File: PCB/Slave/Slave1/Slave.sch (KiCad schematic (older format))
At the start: 42 parts, among them J1 Jack-DC, J10 MH, J11 MH, J12 LED1, J13 LED3, J14 LED5, J15 LED2, J16 LED4, J2 GP_IO, J3 PGM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

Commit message: working on the pcb
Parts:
- removed C10, C2: 1µ, Capacitors_SMD:C_0603_HandSoldering, symbol C
- removed J2: GP_IO, Pin_Headers:Pin_Header_Straight_1x04_Pitch2.54mm, symbol Conn_01x04
- removed J7: PIC_IO, Pin_Headers:Pin_Header_Straight_1x05_Pitch2.54mm, symbol Conn_01x05
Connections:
- net B1: now also U4.6 (LED0); no longer U4.8 (LED2)
- net B2: now also U4.9 (LED3); no longer U4.12 (LED5)
- net B3: now also U4.13 (LED6); no longer U4.15 (LED8)
- net B4: now also U4.16 (LED9); no longer U4.18 (LED11)
- net B5: now also U4.20 (LED12); no longer U4.22 (LED14)
- net GND: now also D2.1 (K)
- net MCP_CS: now also U1.11 (~CS)
- net NRF_MISO: no longer U1.14 (SO)
- net NRF_MOSI: no longer U1.13 (SI)
- net R1: now also U4.8 (LED2); no longer U4.6 (LED0)
- net R2: now also U4.12 (LED5); no longer U4.9 (LED3)
- net R3: now also U4.15 (LED8); no longer U4.13 (LED6)
- net R4: now also U4.18 (LED11); no longer U4.16 (LED9)
- net R5: now also U4.22 (LED14); no longer U4.20 (LED12)
- net SEL_MISO: now also U1.14 (SO)
- net SEL_MOSI: now also U1.13 (SI)
- net at R3.2: now also D2.2 (A)
- net IO1: no longer names the net of U3.2 (AN0/OA2OUT/RA0)
- net IO2: no longer names the net of U3.3 (AN1/C2IN1+/RA1)
- net IO3: no longer names the net of U3.9 (OSC1/CLKI/RA2)
- net IO4: no longer names the net of U3.10 (OSC2/CLKO/RA3)
- net IO5: no longer names the net of U3.12 (CV_REF2O_/RP20/T1CK/RA4)
- net SEL1 renamed Select array/SEL1
- net SEL10 renamed Select array/SEL10
- net SEL11 renamed Select array/SEL11
- net SEL12 renamed Select array/SEL12
- net SEL2 renamed Select array/SEL2
- net SEL3 renamed Select array/SEL3
- net SEL4 renamed Select array/SEL4
- net SEL5 renamed Select array/SEL8
- net SEL6 renamed Select array/SEL7
- net SEL7 renamed Select array/SEL6
- net SEL8 renamed Select array/SEL5
- net SEL9 renamed Select array/SEL9
- no-connect marks 6 -> 15
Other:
- moved on the sheet: J12, J13, J14, J15, J16

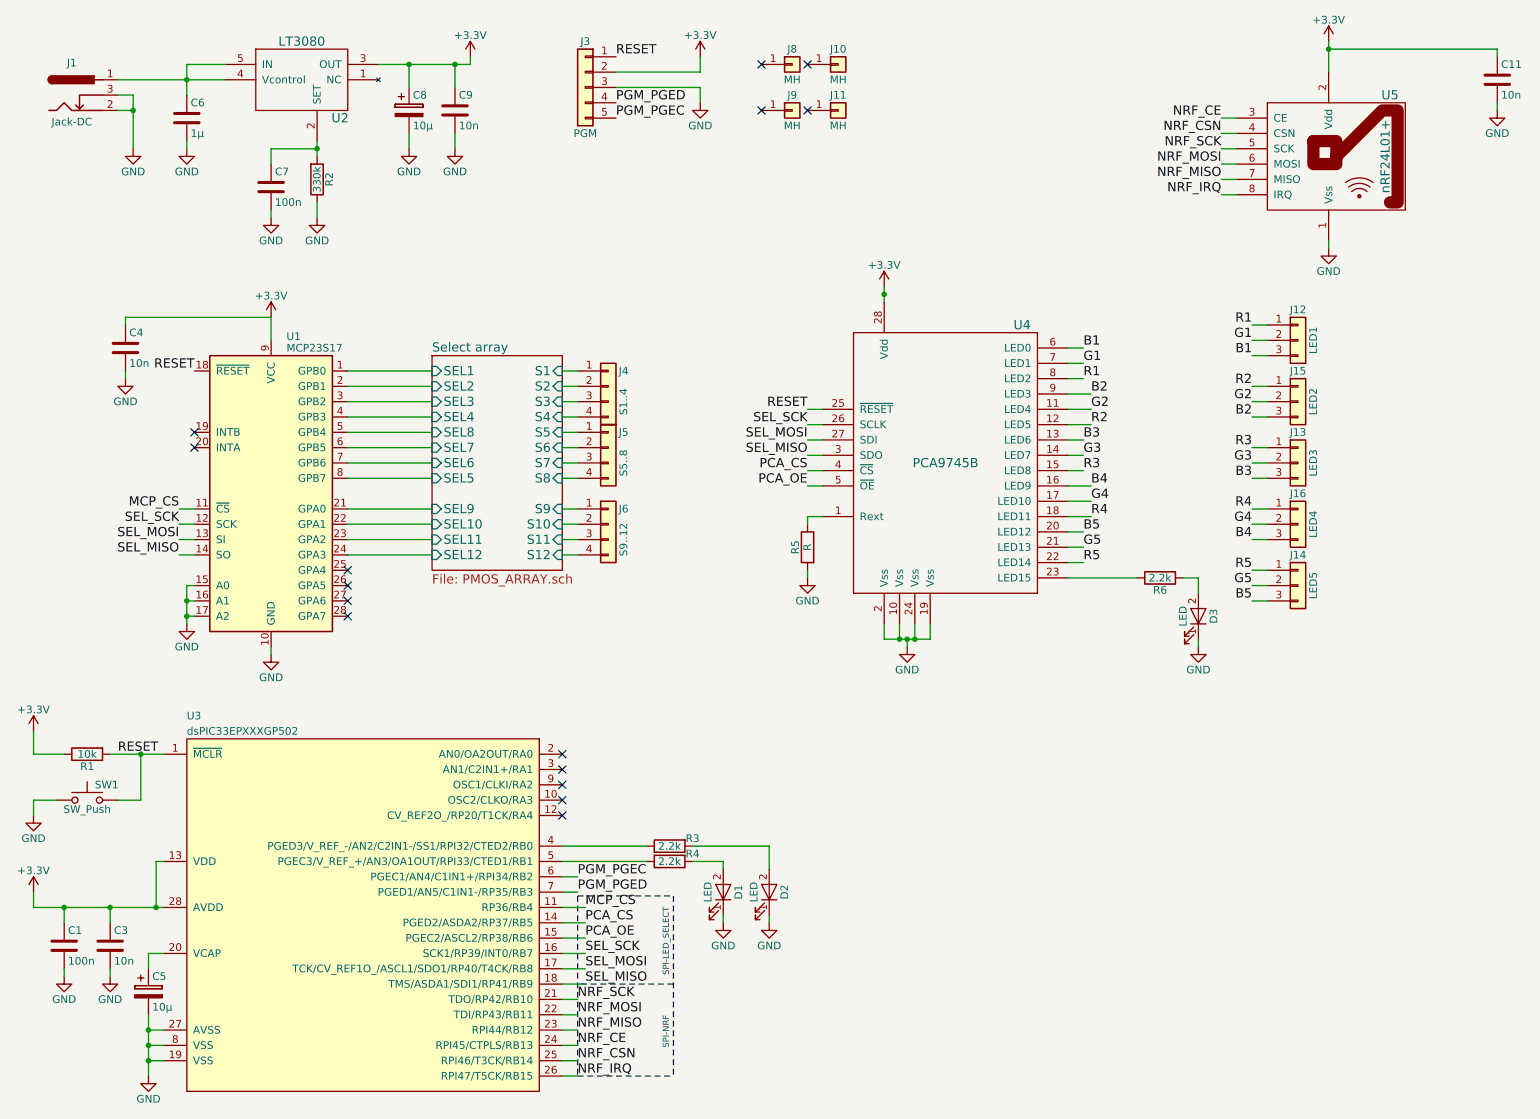
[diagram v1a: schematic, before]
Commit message: created C PIC project for slave
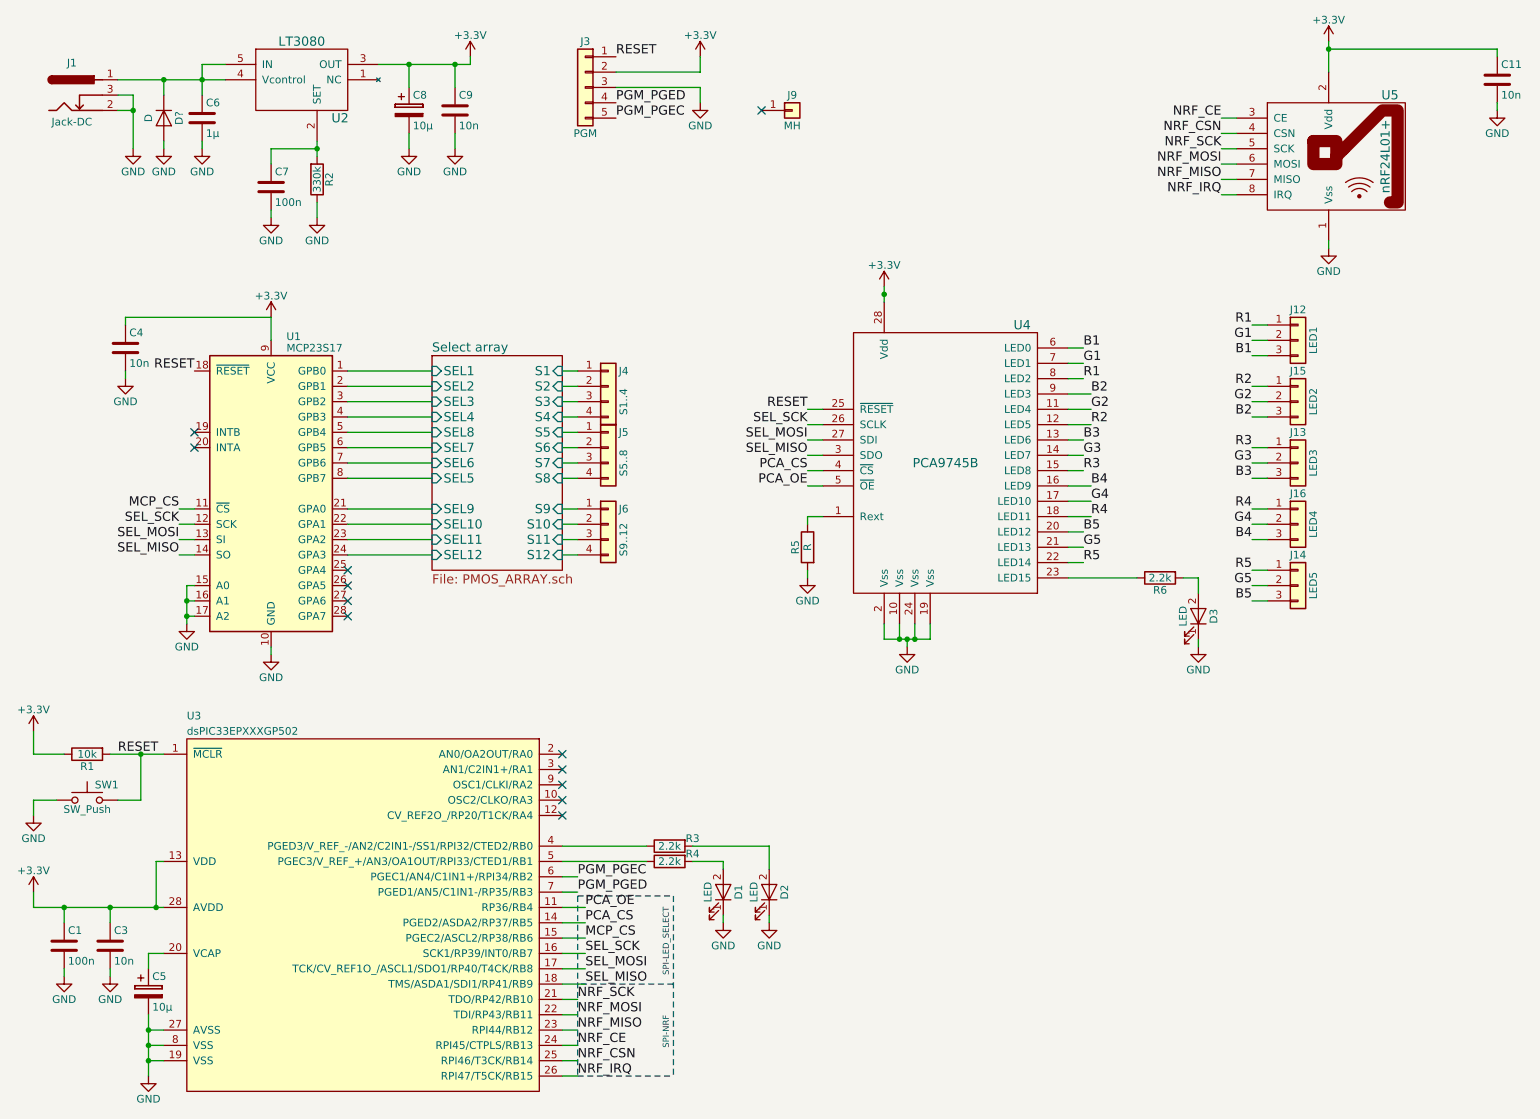
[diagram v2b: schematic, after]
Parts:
- removed J10, J11, J8: MH, Mounting_Holes:MountingHole_2.7mm_M2.5_ISO14580_Pad, symbol Conn_01x01
- added D?: D, Diodes_SMD:D_MicroMELF_Hadsoldering, symbol D
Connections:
- net GND: now also D?.2 (A)
- net MCP_CS: now also U3.15 (PGEC2/ASCL2/RP38/RB6); no longer U3.11 (RP36/RB4)
- net PCA_OE: now also U3.11 (RP36/RB4); no longer U3.15 (PGEC2/ASCL2/RP38/RB6)
- net at C6.1, J1.1, U2.4 (Vcontrol)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: now also D?.1 (K)
- no-connect marks 15 -> 12
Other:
- moved on the sheet: C6
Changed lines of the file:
@@
 Text Label 4500 6550 0    60   ~ 0
 PCA_CS
-Text Label 4500 6650 0    60   ~ 0
+Text Label 4500 6450 0    60   ~ 0
 PCA_OE
 Text Label 5950 3200 2    60   ~ 0
@@
 $EndComp
 $Comp
-L Conn_01x01 J8
-U 1 1 5B16DAF4
-P 5850 950
-F 0 "J8" H 5850 1050 50  0000 C CNN
-F 1 "MH" H 5850 850 50  0000 C CNN
-F 2 "Mounting_Holes:MountingHole_2.7mm_M2.5_ISO14580_Pad" H 5850 950 50  0001 C CNN
-F 3 "" H 5850 950 50  0001 C CNN
-	1    5850 950
-	1    0    0    -1
-$EndComp
-$Comp
-L Conn_01x01 J10
-U 1 1 5B16E03C
-P 6150 950
-F 0 "J10" H 6150 1050 50  0000 C CNN
-F 1 "MH" H 6150 850 50  0000 C CNN
-F 2 "Mounting_Holes:MountingHole_2.7mm_M2.5_ISO14580_Pad" H 6150 950 50  0001 C CNN
-F 3 "" H 6150 950 50  0001 C CNN
-	1    6150 950
-	1    0    0    -1
-$EndComp
-$Comp
 L Conn_01x01 J9
 U 1 1 5B16E0EF
@@
 $EndComp
 $Comp
-L Conn_01x01 J11
-U 1 1 5B16E1A9
-P 6150 1250
-F 0 "J11" H 6150 1350 50  0000 C CNN
-F 1 "MH" H 6150 1150 50  0000 C CNN
-F 2 "Mounting_Holes:MountingHole_2.7mm_M2.5_ISO14580_Pad" H 6150 1250 50  0001 C CNN
-F 3 "" H 6150 1250 50  0001 C CNN
-	1    6150 1250
-	1    0    0    -1
-$EndComp
-$Comp
 L Jack-DC J1
 U 1 1 5B16FEF2
@@
 L C C6
 U 1 1 5B170EA3
-P 1900 1300
-F 0 "C6" H 1925 1400 50  0000 L CNN
-F 1 "1µ" H 1925 1200 50  0000 L CNN
-F 2 "Capacitors_SMD:C_0603_HandSoldering" H 1938 1150 50  0001 C CNN
-F 3 "" H 1900 1300 50  0001 C CNN
-	1    1900 1300
+P 2000 1300
+F 0 "C6" H 2025 1400 50  0000 L CNN
+F 1 "1µ" H 2025 1200 50  0000 L CNN
+F 2 "Capacitors_SMD:C_0603_HandSoldering" H 2038 1150 50  0001 C CNN
+F 3 "" H 2000 1300 50  0001 C CNN
+	1    2000 1300
 	1    0    0    -1
 $EndComp
@@
 L GND #PWR012
 U 1 1 5B171A77
-P 1900 1500
-F 0 "#PWR012" H 1900 1250 50  0001 C CNN
-F 1 "GND" H 1900 1350 50  0000 C CNN
-F 2 "" H 1900 1500 50  0001 C CNN
-F 3 "" H 1900 1500 50  0001 C CNN
-	1    1900 1500
+P 2000 1500
+F 0 "#PWR012" H 2000 1250 50  0001 C CNN
+F 1 "GND" H 2000 1350 50  0000 C CNN
+F 2 "" H 2000 1500 50  0001 C CNN
+F 3 "" H 2000 1500 50  0001 C CNN
+	1    2000 1500
 	1    0    0    -1
 $EndComp
@@
 Text Label 1850 3950 2    60   ~ 0
 SEL_SCK
-Text Label 4500 6450 0    60   ~ 0
+Text Label 4500 6650 0    60   ~ 0
 MCP_CS
 Wire Wire Line
@@
 	1450 1050 2150 1050
 Wire Wire Line
-	2150 950  1900 950
-Wire Wire Line
-	1900 950  1900 1150
-Connection ~ 1900 1050
+	2150 950  2000 950
+Wire Wire Line
+	2000 950  2000 1150
+Connection ~ 2000 1050
 Wire Wire Line
 	3150 950  3750 950
@@
 	3350 1500 3350 1400
 Wire Wire Line
-	1900 1500 1900 1450
+	2000 1500 2000 1450
 Wire Wire Line
 	3750 950  3750 900
@@
 Wire Wire Line
 	4450 4150 4350 4150
-NoConn ~ 5650 950
 NoConn ~ 5650 1250
-NoConn ~ 5950 950
-NoConn ~ 5950 1250
 Wire Wire Line
 	2950 3250 3500 3250
@@
 NoConn ~ 4350 5550
 NoConn ~ 4350 5450
+$Comp
+L D D?
+U 1 1 5B1811C6
+P 1750 1300
+F 0 "D?" H 1750 1400 50  0000 C CNN
+F 1 "D" H 1750 1200 50  0000 C CNN
+F 2 "Diodes_SMD:D_MicroMELF_Hadsoldering" H 1750 1300 50  0001 C CNN
+F 3 "" H 1750 1300 50  0001 C CNN
+	1    1750 1300
+	0    1    1    0
+$EndComp
+$Comp
+L GND #PWR?
+U 1 1 5B1815B1
+P 1750 1500
+F 0 "#PWR?" H 1750 1250 50  0001 C CNN
+F 1 "GND" H 1750 1350 50  0000 C CNN
+F 2 "" H 1750 1500 50  0001 C CNN
+F 3 "" H 1750 1500 50  0001 C CNN
+	1    1750 1500
+	1    0    0    -1
+$EndComp
+Wire Wire Line
+	1750 1500 1750 1450
+Wire Wire Line
+	1750 1150 1750 1050
+Connection ~ 1750 1050
 $EndSCHEMATC

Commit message: better slave pcb
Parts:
- added D17: LED, LEDs:LED_0603_HandSoldering, symbol LED
- added J2: PPIO, Pin_Headers:Pin_Header_Straight_1x04_Pitch2.54mm, symbol Conn_01x04
- added J7: MH, Mounting_Holes:MountingHole_2.7mm_M2.5_ISO14580_Pad, symbol Conn_01x01
- added R43: 2.2k, Resistors_SMD:R_0603_HandSoldering, symbol R
- gave numbers to parts that had none: 1
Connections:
- net GND: now also D17.1 (K)
- net at U3.9 (OSC1/CLKI/RA2): now also R43.1
- net at U1.25 (GPA4): now also J2.1 (Pin_1)
- net at U1.26 (GPA5): now also J2.2 (Pin_2)
- net at U1.27 (GPA6): now also J2.3 (Pin_3)
- net at U1.28 (GPA7): now also J2.4 (Pin_4)
- new net: D17.2 (A), R43.2
- no-connect marks 12 -> 8
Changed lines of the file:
@@
 Wire Wire Line
 	1500 2600 2450 2600
-NoConn ~ 2950 4250
-NoConn ~ 2950 4350
-NoConn ~ 2950 4450
-NoConn ~ 2950 4550
 NoConn ~ 4350 5850
 NoConn ~ 4350 5750
-NoConn ~ 4350 5650
 NoConn ~ 4350 5550
 NoConn ~ 4350 5450
 $Comp
-L D D?
+L D D16
 U 1 1 5B1811C6
 P 1750 1300
-F 0 "D?" H 1750 1400 50  0000 C CNN
+F 0 "D16" H 1750 1400 50  0000 C CNN
 F 1 "D" H 1750 1200 50  0000 C CNN
 F 2 "Diodes_SMD:D_MicroMELF_Hadsoldering" H 1750 1300 50  0001 C CNN
@@
 $EndComp
 $Comp
-L GND #PWR?
+L GND #PWR029
 U 1 1 5B1815B1
 P 1750 1500
-F 0 "#PWR?" H 1750 1250 50  0001 C CNN
+F 0 "#PWR029" H 1750 1250 50  0001 C CNN
 F 1 "GND" H 1750 1350 50  0000 C CNN
 F 2 "" H 1750 1500 50  0001 C CNN
@@
 	1750 1150 1750 1050
 Connection ~ 1750 1050
+$Comp
+L R R43
+U 1 1 5B1E3DB6
+P 5050 5650
+F 0 "R43" V 5000 5500 50  0000 C CNN
+F 1 "2.2k" V 5050 5650 50  0000 C CNN
+F 2 "Resistors_SMD:R_0603_HandSoldering" V 4980 5650 50  0001 C CNN
+F 3 "" H 5050 5650 50  0001 C CNN
+	1    5050 5650
+	0    -1   1    0
+$EndComp
+$Comp
+L LED D17
+U 1 1 5B1E409C
+P 6000 6350
+F 0 "D17" H 6000 6450 50  0000 C CNN
+F 1 "LED" H 6000 6250 50  0000 C CNN
+F 2 "LEDs:LED_0603_HandSoldering" H 6000 6350 50  0001 C CNN
+F 3 "" H 6000 6350 50  0001 C CNN
+	1    6000 6350
+	0    1    -1   0
+$EndComp
+$Comp
+L GND #PWR030
+U 1 1 5B1E41BE
+P 6000 6550
+F 0 "#PWR030" H 6000 6300 50  0001 C CNN
+F 1 "GND" H 6000 6400 50  0000 C CNN
+F 2 "" H 6000 6550 50  0001 C CNN
+F 3 "" H 6000 6550 50  0001 C CNN
+	1    6000 6550
+	1    0    0    -1
+$EndComp
+Wire Wire Line
+	6000 6550 6000 6500
+Wire Wire Line
+	6000 6200 6000 5650
+Wire Wire Line
+	6000 5650 5200 5650
+Wire Wire Line
+	4350 5650 4900 5650
+$Comp
+L Conn_01x04 J2
+U 1 1 5B1E64E5
+P 3250 4350
+F 0 "J2" H 3350 4450 50  0000 C CNN
+F 1 "PPIO" V 3350 4250 50  0000 C CNN
+F 2 "Pin_Headers:Pin_Header_Straight_1x04_Pitch2.54mm" H 3250 4350 50  0001 C CNN
+F 3 "" H 3250 4350 50  0001 C CNN
+	1    3250 4350
+	1    0    0    -1
+$EndComp
+Wire Wire Line
+	3050 4250 2950 4250
+Wire Wire Line
+	2950 4350 3050 4350
+Wire Wire Line
+	2950 4450 3050 4450
+Wire Wire Line
+	2950 4550 3050 4550
+$Comp
+L Conn_01x01 J7
+U 1 1 5B1E7ED5
+P 6250 1250
+F 0 "J7" H 6250 1350 50  0000 C CNN
+F 1 "MH" H 6250 1150 50  0000 C CNN
+F 2 "Mounting_Holes:MountingHole_2.7mm_M2.5_ISO14580_Pad" H 6250 1250 50  0001 C CNN
+F 3 "" H 6250 1250 50  0001 C CNN
+	1    6250 1250
+	1    0    0    -1
+$EndComp
+NoConn ~ 6050 1250
 $EndSCHEMATC

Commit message: updated pcb for prototype
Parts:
- removed J1: Jack-DC, Connect:BARREL_JACK, symbol Jack-DC
- added J1: 5V, Pin_Headers:Pin_Header_Straight_1x02_Pitch2.54mm, symbol Conn_01x02
- added SW2: SW_Push_SPDT, Pin_Headers:Pin_Header_Straight_1x03_Pitch2.54mm, symbol SW_Push_SPDT
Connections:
- net +3V3: now also SW2.1 (A)
- net GND: now also J1.2 (Pin_2)
- net +5V: now reaches C6.1, D16.1 (K), U2.4 (Vcontrol), U2.5 (IN)
- net +5V: now also J1.1 (Pin_1), SW2.3 (C)
- new net Select array/Vdd: SW2.2 (B)
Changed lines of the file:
@@
-$EndComp
-$Comp
-L Jack-DC J1
-U 1 1 5B16FEF2
-P 1150 1150
-F 0 "J1" H 1150 1360 50  0000 C CNN
-F 1 "Jack-DC" H 1150 975 50  0000 C CNN
-F 2 "Connect:BARREL_JACK" H 1200 1110 50  0001 C CNN
-F 3 "" H 1200 1110 50  0001 C CNN
-	1    1150 1150
-	1    0    0    -1
 $EndComp
 $Comp
@@
 	1550 1150 1450 1150
 Wire Wire Line
-	1450 1250 1550 1250
-Connection ~ 1550 1250
-Wire Wire Line
 	1450 1050 2150 1050
 Wire Wire Line
 	2150 950  2000 950
 Wire Wire Line
-	2000 950  2000 1150
+	2000 900  2000 1150
 Connection ~ 2000 1050
 Wire Wire Line
@@
 	5400 6150 5400 6200
 $Sheet
-S 3500 2850 850  1400
+S 3500 2850 850  1500
 U 5B180A3C
 F0 "Select array" 60
@@
 F24 "SEL12" I L 3500 4150 60
 F25 "S12" I R 4350 4150 60
+F26 "Vdd" I R 4350 4300 60
 $EndSheet
 $Comp
@@
 $EndComp
 NoConn ~ 6050 1250
+$Comp
+L +5V #PWR031
+U 1 1 5B45643A
+P 2000 900
+F 0 "#PWR031" H 2000 750 50  0001 C CNN
+F 1 "+5V" H 2000 1040 50  0000 C CNN
+F 2 "" H 2000 900 50  0001 C CNN
+F 3 "" H 2000 900 50  0001 C CNN
+	1    2000 900
+	1    0    0    -1
+$EndComp
+Connection ~ 2000 950
+$Comp
+L SW_Push_SPDT SW2
+U 1 1 5B456FB5
+P 4950 4300
+F 0 "SW2" H 4950 4470 50  0000 C CNN
+F 1 "SW_Push_SPDT" H 4950 4100 50  0000 C CNN
+F 2 "Pin_Headers:Pin_Header_Straight_1x03_Pitch2.54mm" H 4950 4300 50  0001 C CNN
+F 3 "" H 4950 4300 50  0001 C CNN
+	1    4950 4300
+	1    0    0    -1
+$EndComp
+$Comp
+L +3.3V #PWR032
+U 1 1 5B45740B
+P 5250 4150
+F 0 "#PWR032" H 5250 4000 50  0001 C CNN
+F 1 "+3.3V" H 5250 4290 50  0000 C CNN
+F 2 "" H 5250 4150 50  0001 C CNN
+F 3 "" H 5250 4150 50  0001 C CNN
+	1    5250 4150
+	1    0    0    -1
+$EndComp
+$Comp
+L +5V #PWR033
+U 1 1 5B457F93
+P 5300 4350
+F 0 "#PWR033" H 5300 4200 50  0001 C CNN
+F 1 "+5V" H 5300 4490 50  0000 C CNN
+F 2 "" H 5300 4350 50  0001 C CNN
+F 3 "" H 5300 4350 50  0001 C CNN
+	1    5300 4350
+	1    0    0    -1
+$EndComp
+Wire Wire Line
+	5150 4200 5250 4200
+Wire Wire Line
+	5250 4200 5250 4150
+Wire Wire Line
+	5150 4400 5300 4400
+Wire Wire Line
+	5300 4400 5300 4350
+Wire Wire Line
+	4750 4300 4350 4300
+$Comp
+L Conn_01x02 J1
+U 1 1 5B459B50
+P 1250 1050
+F 0 "J1" H 1250 1150 50  0000 C CNN
+F 1 "5V" H 1250 850 50  0000 C CNN
+F 2 "Pin_Headers:Pin_Header_Straight_1x02_Pitch2.54mm" H 1250 1050 50  0001 C CNN
+F 3 "" H 1250 1050 50  0001 C CNN
+	1    1250 1050
+	-1   0    0    -1
+$EndComp
 $EndSCHEMATC
